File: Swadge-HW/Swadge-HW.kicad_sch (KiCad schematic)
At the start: 178 parts, among them J1 Conn_02x03_Odd_Even, J2 PJ-307C, J3 Conn_01x05_Male, P1 USB_C_Plug_USB2.0, Q1 Q_PMOS_GSD, SW1 YTS-D003-1A, SW2 YTS-D003-1A, SW3 YTS-D003-1A, SW4 YTS-D003-1A, SW5 YTS-D003-1A, SW6 YTS-D003-1A, SW7 TS-1103S-B-B, SW8 TS-1103S-B-B, SW9 SW_SPDT_1825232-1, U1 ESP32-S2-MINI-1, U11 CH32V003F4U6, U2 RB017A1505A, U3 M3410, U5 RB017A1505A_Connector, U6 LSM6DSL, U7 GENERIC_LDO_GOI, U8 FM8002A, U9 INGHAi_GSPK2307P-8R1W

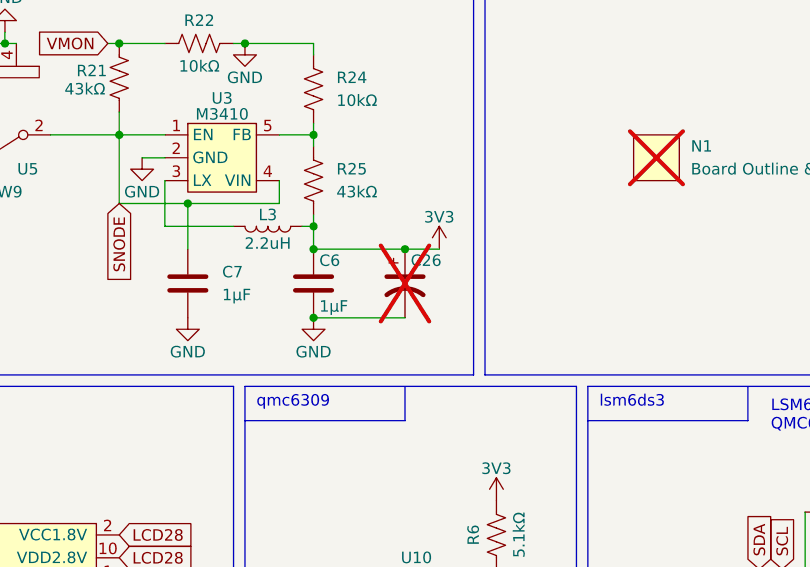
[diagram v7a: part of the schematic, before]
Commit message: Add gear art, signature Remove silk from top Add more vias Populate C26, 3D model
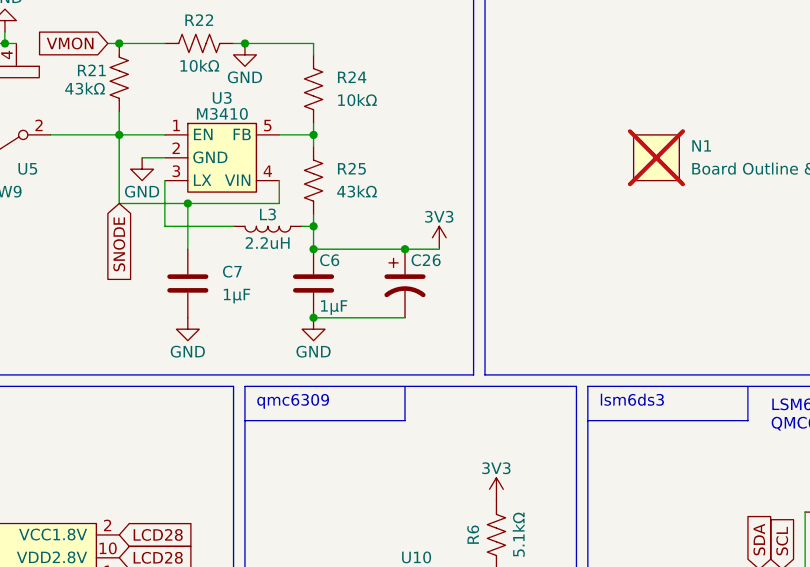
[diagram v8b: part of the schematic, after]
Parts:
- C26: value C_Polarized_US -> 470uF; now fitted
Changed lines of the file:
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@@
 		(in_bom yes)
 		(on_board yes)
-		(dnp yes)
+		(dnp no)
 		(property "Reference" "C26"
 			(at 167.005 190.5 0)
@@
 			)
 		)
-		(property "Value" "C_Polarized_US"
+		(property "Value" "470uF"
 			(at 167.005 195.58 0)
 			(effects
@@
 			(at 166.37 193.04 0)
 			(effects
-				(font
-					(size 1.27 1.27)
-				)
-				(hide yes)
-			)
-		)
-		(property "Cost@2500" ""
-			(at 166.37 193.04 0)
-			(effects
